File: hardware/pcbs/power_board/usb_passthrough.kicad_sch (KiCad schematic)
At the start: 2 parts

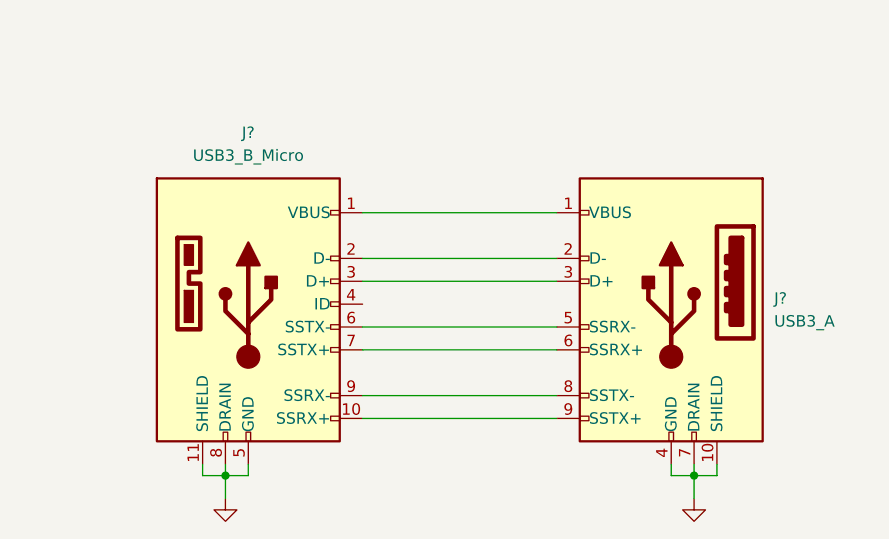
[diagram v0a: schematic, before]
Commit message: power_board: minor fixes to shematic
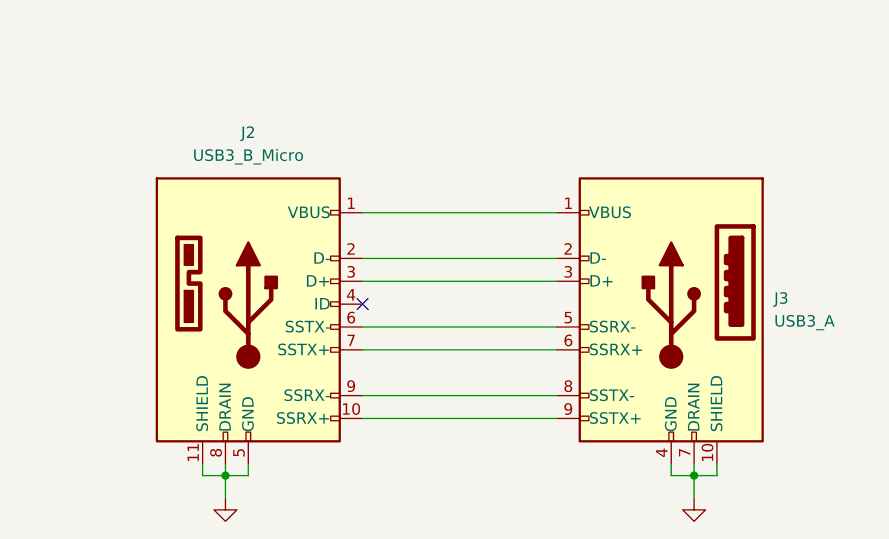
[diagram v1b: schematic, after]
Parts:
- gave numbers to parts that had none: 2
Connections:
- no-connect marks 0 -> 1
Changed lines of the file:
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@@
   (junction (at 138.43 114.3) (diameter 0) (color 0 0 0 0)
   )
+  (no_connect (at 153.67 95.25))
   (wire (pts (xy 153.67 100.33) (xy 175.26 100.33))
     (stroke (width 0) (type default))
@@
   (symbol (lib_id "Connector:USB3_B_Micro") (at 140.97 95.25 0) (unit 1)
     (in_bom yes) (on_board yes) (dnp no) (fields_autoplaced)
-    (property "Reference" "J?" (at 140.97 76.2 0)
+    (property "Reference" "J2" (at 140.97 76.2 0)
       (effects (font (size 1.27 1.27)))
     )
@@
       (project "power_board"
         (path "/4b166175-80a4-48c6-994d-6e62a6160b87/91441b40-0438-4eff-8649-c295c7239fb6"
-          (reference "J?") (unit 1)
+          (reference "J2") (unit 1)
         )
       )
@@
   (symbol (lib_id "power:GND") (at 138.43 116.84 0) (unit 1)
     (in_bom yes) (on_board yes) (dnp no) (fields_autoplaced)
-    (property "Reference" "#PWR01" (at 138.43 123.19 0)
+    (property "Reference" "#PWR06" (at 138.43 123.19 0)
       (effects (font (size 1.27 1.27)) hide)
     )
@@
       (project "power_board"
         (path "/4b166175-80a4-48c6-994d-6e62a6160b87/91441b40-0438-4eff-8649-c295c7239fb6"
-          (reference "#PWR01") (unit 1)
+          (reference "#PWR06") (unit 1)
         )
       )
@@
   (symbol (lib_id "power:GND") (at 190.5 116.84 0) (unit 1)
     (in_bom yes) (on_board yes) (dnp no) (fields_autoplaced)
-    (property "Reference" "#PWR02" (at 190.5 123.19 0)
+    (property "Reference" "#PWR07" (at 190.5 123.19 0)
       (effects (font (size 1.27 1.27)) hide)
     )
@@
       (project "power_board"
         (path "/4b166175-80a4-48c6-994d-6e62a6160b87/91441b40-0438-4eff-8649-c295c7239fb6"
-          (reference "#PWR02") (unit 1)
+          (reference "#PWR07") (unit 1)
         )
       )
@@
   (symbol (lib_id "Connector:USB3_A") (at 187.96 95.25 0) (mirror y) (unit 1)
     (in_bom yes) (on_board yes) (dnp no) (fields_autoplaced)
-    (property "Reference" "J?" (at 199.39 94.615 0)
+    (property "Reference" "J3" (at 199.39 94.615 0)
       (effects (font (size 1.27 1.27)) (justify right))
     )
@@
       (project "power_board"
         (path "/4b166175-80a4-48c6-994d-6e62a6160b87/91441b40-0438-4eff-8649-c295c7239fb6"
-          (reference "J?") (unit 1)
+          (reference "J3") (unit 1)
         )
       )

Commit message: power_board: connect power led to SBC's usb and fix inductor values
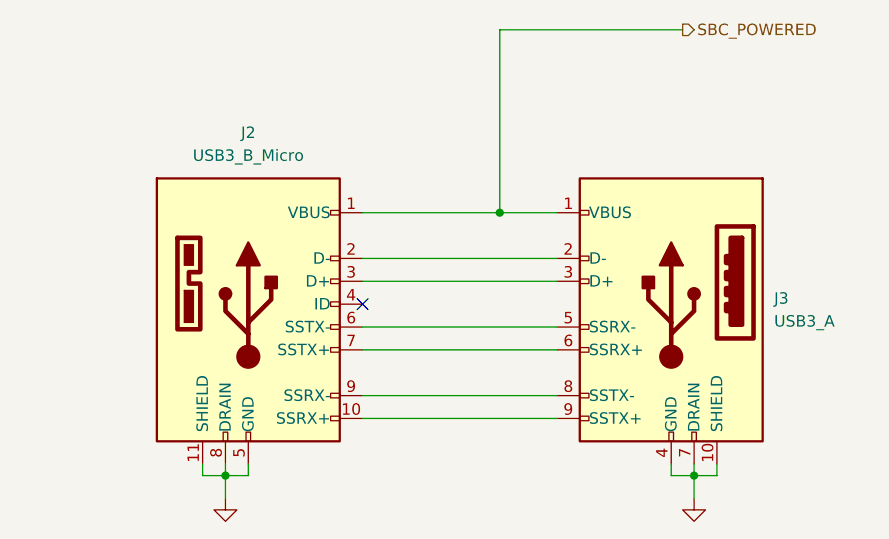
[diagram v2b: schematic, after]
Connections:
- net SBC_POWERED: now reaches J2.1 (VBUS), J3.1 (VBUS)
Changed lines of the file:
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@@
   (junction (at 138.43 114.3) (diameter 0) (color 0 0 0 0)
+  )
+  (junction (at 168.91 85.09) (diameter 0) (color 0 0 0 0)
   )
   (no_connect (at 153.67 95.25))
@@
     (stroke (width 0) (type default))
   )
-  (wire (pts (xy 153.67 85.09) (xy 175.26 85.09))
+  (wire (pts (xy 153.67 85.09) (xy 168.91 85.09))
+    (stroke (width 0) (type default))
+  )
+  (wire (pts (xy 168.91 85.09) (xy 175.26 85.09))
     (stroke (width 0) (type default))
   )
@@
     (stroke (width 0) (type default))
   )
+  (wire (pts (xy 189.23 64.77) (xy 168.91 64.77))
+    (stroke (width 0) (type default))
+  )
   (wire (pts (xy 190.5 113.03) (xy 190.5 114.3))
     (stroke (width 0) (type default))
@@
   )
   (wire (pts (xy 190.5 114.3) (xy 190.5 116.84))
+    (stroke (width 0) (type default))
+  )
+  (wire (pts (xy 168.91 64.77) (xy 168.91 85.09))
     (stroke (width 0) (type default))
   )
@@
     (stroke (width 0) (type default))
   )
+  (hierarchical_label "SBC_POWERED" (shape output) (at 189.23 64.77 0) (fields_autoplaced)
+    (effects (font (size 1.27 1.27)) (justify left))
+  )
   (symbol (lib_id "Connector:USB3_B_Micro") (at 140.97 95.25 0) (unit 1)

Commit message: power_board: finalise all footprints
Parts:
- added C1: 1μF, Capacitor_SMD:C_0805_2012Metric, symbol Device:C
- J2: footprint (none) -> Connector_USB:USB3_Micro-B_Connfly_DS1104-01; symbol Connector:USB3_B_Micro -> conn:USB3_B_Micro_PassiveGND
- J3: footprint (none) -> conn:USB3_A_Amphenol_GSB3111XXXHR
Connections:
- net GND: now also C1.2
- net SBC_POWERED: now also C1.1
- net at J2.10 (SSRX+): now also J3.6 (SSRX+); no longer J3.9 (SSTX+)
- net at J2.6 (SSTX-): now also J3.8 (SSTX-); no longer J3.5 (SSRX-)
- net at J2.7 (SSTX+): now also J3.9 (SSTX+); no longer J3.6 (SSRX+)
- net at J2.9 (SSRX-): now also J3.5 (SSRX-); no longer J3.8 (SSTX-)
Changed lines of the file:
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@@
 (kicad_sch (version 20230121) (generator eeschema)
   (paper "A4")
+  (junction (at 163.83 71.12) (diameter 0) (color 0 0 0 0)
+  )
+  (junction (at 172.72 71.12) (diameter 0) (color 0 0 0 0)
+  )
   (junction (at 190.5 114.3) (diameter 0) (color 0 0 0 0)
   )
   (junction (at 138.43 114.3) (diameter 0) (color 0 0 0 0)
   )
-  (junction (at 168.91 85.09) (diameter 0) (color 0 0 0 0)
-  )
   (no_connect (at 153.67 95.25))
-  (wire (pts (xy 153.67 100.33) (xy 175.26 100.33))
-    (stroke (width 0) (type default))
-  )
-  (wire (pts (xy 153.67 85.09) (xy 168.91 85.09))
-    (stroke (width 0) (type default))
-  )
-  (wire (pts (xy 168.91 85.09) (xy 175.26 85.09))
+  (wire (pts (xy 153.67 97.79) (xy 162.56 97.79))
     (stroke (width 0) (type default))
   )
@@
     (stroke (width 0) (type default))
   )
-  (wire (pts (xy 153.67 107.95) (xy 175.26 107.95))
+  (wire (pts (xy 163.83 82.55) (xy 163.83 86.36))
+    (stroke (width 0) (type default))
+  )
+  (wire (pts (xy 156.21 85.09) (xy 156.21 71.12))
+    (stroke (width 0) (type default))
+  )
+  (wire (pts (xy 170.18 105.41) (xy 162.56 97.79))
+    (stroke (width 0) (type default))
+  )
+  (wire (pts (xy 167.64 97.79) (xy 175.26 97.79))
     (stroke (width 0) (type default))
   )
@@
     (stroke (width 0) (type default))
   )
-  (wire (pts (xy 189.23 64.77) (xy 168.91 64.77))
+  (wire (pts (xy 172.72 85.09) (xy 175.26 85.09))
+    (stroke (width 0) (type default))
+  )
+  (wire (pts (xy 163.83 71.12) (xy 172.72 71.12))
+    (stroke (width 0) (type default))
+  )
+  (wire (pts (xy 153.67 105.41) (xy 160.02 105.41))
+    (stroke (width 0) (type default))
+  )
+  (wire (pts (xy 153.67 85.09) (xy 156.21 85.09))
+    (stroke (width 0) (type default))
+  )
+  (wire (pts (xy 172.72 71.12) (xy 172.72 85.09))
+    (stroke (width 0) (type default))
+  )
+  (wire (pts (xy 153.67 107.95) (xy 162.56 107.95))
+    (stroke (width 0) (type default))
+  )
+  (wire (pts (xy 193.04 71.12) (xy 172.72 71.12))
     (stroke (width 0) (type default))
   )
@@
     (stroke (width 0) (type default))
   )
-  (wire (pts (xy 168.91 64.77) (xy 168.91 85.09))
+  (wire (pts (xy 170.18 100.33) (xy 175.26 100.33))
     (stroke (width 0) (type default))
   )
@@
     (stroke (width 0) (type default))
   )
+  (wire (pts (xy 160.02 105.41) (xy 167.64 97.79))
+    (stroke (width 0) (type default))
+  )
+  (wire (pts (xy 163.83 71.12) (xy 163.83 74.93))
+    (stroke (width 0) (type default))
+  )
   (wire (pts (xy 140.97 114.3) (xy 140.97 113.03))
     (stroke (width 0) (type default))
   )
-  (wire (pts (xy 153.67 97.79) (xy 175.26 97.79))
+  (wire (pts (xy 170.18 100.33) (xy 162.56 107.95))
+    (stroke (width 0) (type default))
+  )
+  (wire (pts (xy 156.21 71.12) (xy 163.83 71.12))
     (stroke (width 0) (type default))
   )
@@
     (stroke (width 0) (type default))
   )
-  (wire (pts (xy 153.67 105.41) (xy 175.26 105.41))
+  (wire (pts (xy 153.67 100.33) (xy 160.02 100.33))
+    (stroke (width 0) (type default))
+  )
+  (wire (pts (xy 160.02 100.33) (xy 167.64 107.95))
+    (stroke (width 0) (type default))
+  )
+  (wire (pts (xy 167.64 107.95) (xy 175.26 107.95))
     (stroke (width 0) (type default))
   )
@@
     (stroke (width 0) (type default))
   )
+  (wire (pts (xy 170.18 105.41) (xy 175.26 105.41))
+    (stroke (width 0) (type default))
+  )
   (wire (pts (xy 187.96 114.3) (xy 190.5 114.3))
     (stroke (width 0) (type default))
@@
     (stroke (width 0) (type default))
   )
-  (hierarchical_label "SBC_POWERED" (shape output) (at 189.23 64.77 0) (fields_autoplaced)
+  (hierarchical_label "SBC_POWERED" (shape output) (at 193.04 71.12 0) (fields_autoplaced)
     (effects (font (size 1.27 1.27)) (justify left))
   )
-  (symbol (lib_id "Connector:USB3_B_Micro") (at 140.97 95.25 0) (unit 1)
+  (symbol (lib_id "Device:C") (at 163.83 78.74 0) (unit 1)
+    (in_bom yes) (on_board yes) (dnp no)
+    (property "Reference" "C1" (at 165.1 76.2 0)
+      (effects (font (size 1.27 1.27)) (justify left))
+    )
+    (property "Value" "1μF" (at 165.1 81.28 0)
+      (effects (font (size 1.27 1.27)) (justify left))
+    )
+    (property "Footprint" "Capacitor_SMD:C_0805_2012Metric" (at 164.7952 82.55 0)
+      (effects (font (size 1.27 1.27)) hide)
+    )
+    (property "Datasheet" "~" (at 163.83 78.74 0)
+      (effects (font (size 1.27 1.27)) hide)
+    )
+    (property "Info" "16V" (at 165.1 83.82 0)
+      (effects (font (size 1.27 1.27)) (justify left))
+    )
+    (property "Shop" "https://store.comet.bg/Catalogue/Product/16789/" (at 163.83 78.74 0)
+      (effects (font (size 1.27 1.27)) hide)
+    )
+    (pin "1")
+    (pin "2")
+    (instances
+      (project "power_board"
+        (path "/4b166175-80a4-48c6-994d-6e62a6160b87/91441b40-0438-4eff-8649-c295c7239fb6"
+          (reference "C1") (unit 1)
+        )
+      )
+    )
+  )
+  (symbol (lib_id "conn:USB3_B_Micro_PassiveGND") (at 140.97 95.25 0) (unit 1)
     (in_bom yes) (on_board yes) (dnp no) (fields_autoplaced)
     (property "Reference" "J2" (at 140.97 76.2 0)
@@
       (effects (font (size 1.27 1.27)))
     )
-    (property "Footprint" "" (at 144.78 91.44 0)
+    (property "Footprint" "Connector_USB:USB3_Micro-B_Connfly_DS1104-01" (at 144.78 91.44 0)
       (effects (font (size 1.27 1.27)) hide)
     )
@@
   (symbol (lib_id "power:GND") (at 190.5 116.84 0) (unit 1)
     (in_bom yes) (on_board yes) (dnp no) (fields_autoplaced)
-    (property "Reference" "#PWR07" (at 190.5 123.19 0)
+    (property "Reference" "#PWR08" (at 190.5 123.19 0)
       (effects (font (size 1.27 1.27)) hide)
     )
@@
       (project "power_board"
         (path "/4b166175-80a4-48c6-994d-6e62a6160b87/91441b40-0438-4eff-8649-c295c7239fb6"
-          (reference "#PWR07") (unit 1)
+          (reference "#PWR08") (unit 1)
         )
       )
@@
       (effects (font (size 1.27 1.27)) (justify right))
     )
-    (property "Footprint" "" (at 184.15 92.71 0)
+    (property "Footprint" "conn:USB3_A_Amphenol_GSB3111XXXHR" (at 184.15 92.71 0)
       (effects (font (size 1.27 1.27)) hide)
     )
@@
         )
       )
+    )
+  )
+  (symbol (lib_id "power:GND") (at 163.83 86.36 0) (unit 1)
+    (in_bom yes) (on_board yes) (dnp no) (fields_autoplaced)
+    (property "Reference" "#PWR07" (at 163.83 92.71 0)
+      (effects (font (size 1.27 1.27)) hide)
+    )
+    (property "Value" "GND" (at 163.83 91.44 0)
+      (effects (font (size 1.27 1.27)) hide)
+    )
+    (property "Footprint" "" (at 163.83 86.36 0)
+      (effects (font (size 1.27 1.27)) hide)
+    )
+    (property "Datasheet" "" (at 163.83 86.36 0)
+      (effects (font (size 1.27 1.27)) hide)
+    )
+    (pin "1")
+    (instances
+      (project "power_board"
+        (path "/4b166175-80a4-48c6-994d-6e62a6160b87/91441b40-0438-4eff-8649-c295c7239fb6"
+          (reference "#PWR07") (unit 1)
+        )
+      )

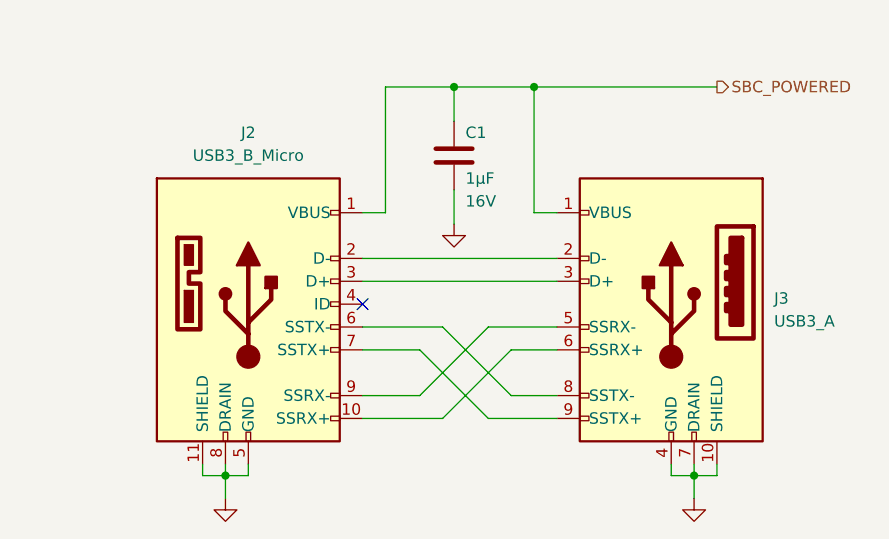
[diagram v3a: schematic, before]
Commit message: power_board: arrange front panel components
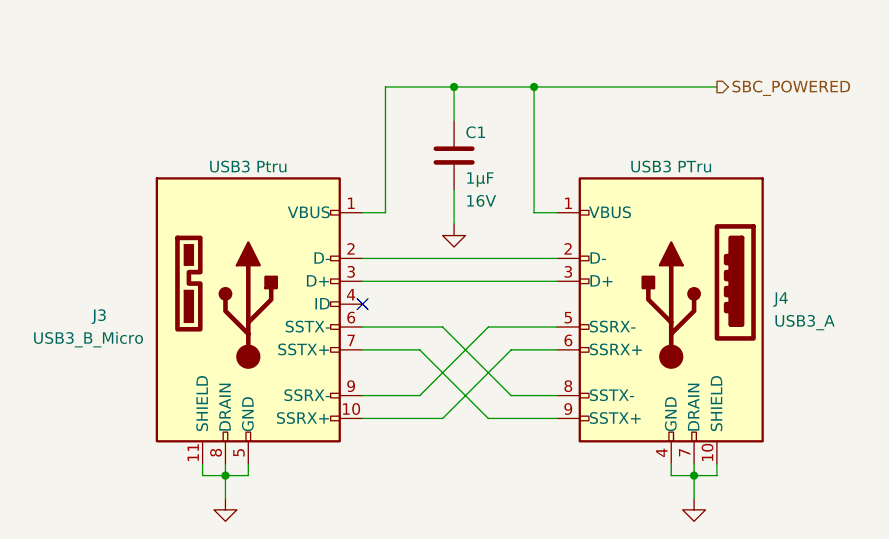
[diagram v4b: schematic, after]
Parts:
- J3: renamed from J2; Purpose (none) -> USB3 Ptru
- J4: renamed from J3; Purpose (none) -> USB3 PTru
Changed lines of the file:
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@@
   )
   (symbol (lib_id "conn:USB3_B_Micro_PassiveGND") (at 140.97 95.25 0) (unit 1)
-    (in_bom yes) (on_board yes) (dnp no) (fields_autoplaced)
-    (property "Reference" "J2" (at 140.97 76.2 0)
+    (in_bom yes) (on_board yes) (dnp no)
+    (property "Reference" "J3" (at 124.46 96.52 0)
       (effects (font (size 1.27 1.27)))
     )
-    (property "Value" "USB3_B_Micro" (at 140.97 78.74 0)
+    (property "Value" "USB3_B_Micro" (at 123.19 99.06 0)
       (effects (font (size 1.27 1.27)))
     )
@@
     (property "Shop" "https://eu.mouser.com/ProductDetail/Amphenol-Commercial-Products/GSB343K33AHR?qs=8nwx9VzGl4ytGKVAGQNj7w%3D%3D" (at 140.97 95.25 0)
       (effects (font (size 1.27 1.27)) hide)
+    )
+    (property "Purpose" "USB3 Ptru" (at 140.97 80.01 0)
+      (effects (font (size 1.27 1.27)))
     )
     (pin "4")
@@
       (project "power_board"
         (path "/4b166175-80a4-48c6-994d-6e62a6160b87/91441b40-0438-4eff-8649-c295c7239fb6"
-          (reference "J2") (unit 1)
+          (reference "J3") (unit 1)
         )
       )
@@
   (symbol (lib_id "power:GND") (at 138.43 116.84 0) (unit 1)
     (in_bom yes) (on_board yes) (dnp no) (fields_autoplaced)
-    (property "Reference" "#PWR06" (at 138.43 123.19 0)
+    (property "Reference" "#PWR07" (at 138.43 123.19 0)
       (effects (font (size 1.27 1.27)) hide)
     )
@@
       (project "power_board"
         (path "/4b166175-80a4-48c6-994d-6e62a6160b87/91441b40-0438-4eff-8649-c295c7239fb6"
-          (reference "#PWR06") (unit 1)
+          (reference "#PWR07") (unit 1)
         )
       )
@@
   (symbol (lib_id "power:GND") (at 190.5 116.84 0) (unit 1)
     (in_bom yes) (on_board yes) (dnp no) (fields_autoplaced)
-    (property "Reference" "#PWR08" (at 190.5 123.19 0)
+    (property "Reference" "#PWR09" (at 190.5 123.19 0)
       (effects (font (size 1.27 1.27)) hide)
     )
@@
       (project "power_board"
         (path "/4b166175-80a4-48c6-994d-6e62a6160b87/91441b40-0438-4eff-8649-c295c7239fb6"
-          (reference "#PWR08") (unit 1)
+          (reference "#PWR09") (unit 1)
         )
       )
@@
   )
   (symbol (lib_id "Connector:USB3_A") (at 187.96 95.25 0) (mirror y) (unit 1)
-    (in_bom yes) (on_board yes) (dnp no) (fields_autoplaced)
-    (property "Reference" "J3" (at 199.39 94.615 0)
+    (in_bom yes) (on_board yes) (dnp no)
+    (property "Reference" "J4" (at 199.39 94.615 0)
       (effects (font (size 1.27 1.27)) (justify right))
     )
@@
       (effects (font (size 1.27 1.27)) hide)
     )
+    (property "Purpose" "USB3 PTru" (at 187.96 80.01 0)
+      (effects (font (size 1.27 1.27)))
+    )
     (pin "9")
     (pin "1")
@@
       (project "power_board"
         (path "/4b166175-80a4-48c6-994d-6e62a6160b87/91441b40-0438-4eff-8649-c295c7239fb6"
-          (reference "J3") (unit 1)
+          (reference "J4") (unit 1)
         )
       )
@@
   (symbol (lib_id "power:GND") (at 163.83 86.36 0) (unit 1)
     (in_bom yes) (on_board yes) (dnp no) (fields_autoplaced)
-    (property "Reference" "#PWR07" (at 163.83 92.71 0)
+    (property "Reference" "#PWR08" (at 163.83 92.71 0)
       (effects (font (size 1.27 1.27)) hide)
     )
@@
       (project "power_board"
         (path "/4b166175-80a4-48c6-994d-6e62a6160b87/91441b40-0438-4eff-8649-c295c7239fb6"
-          (reference "#PWR07") (unit 1)
+          (reference "#PWR08") (unit 1)
         )
       )

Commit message: use a sideways usb connector for USB-3
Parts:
- J4: footprint conn:USB3_A_Amphenol_GSB3111XXXHR -> conn:USB3_A_Amphenol_GSB3116344KHHR; Shop https://eu.mouser.com/ProductDetail/Amphenol-Commercial-Products/GSB3111311HR?qs=f9yNj16SXrLtdMOGrQx7ow%3D%3D -> https://eu.mouser.com/ProductDetail/Amphenol-Commercial-Products/GSB3116344KHHR?qs=81r%252BiQLm7BSSapR8R%252Bkfyg%3D%3D
